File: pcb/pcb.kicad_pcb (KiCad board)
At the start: 2 copper layers, 69.8 x 69.8 mm, 61 parts, among them J1 USB_C_Receptacle_USB2.0, J2 Conn_01x05, SW1 SW_Push, SW2 SW_Push, U1 XC6206P332MR, U2 SRV05-4, U3 DRV5056A3xDBZxQ1, U4 DRV5056A3xDBZxQ1, U5 DRV5056A3xDBZxQ1, U6 RP2040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

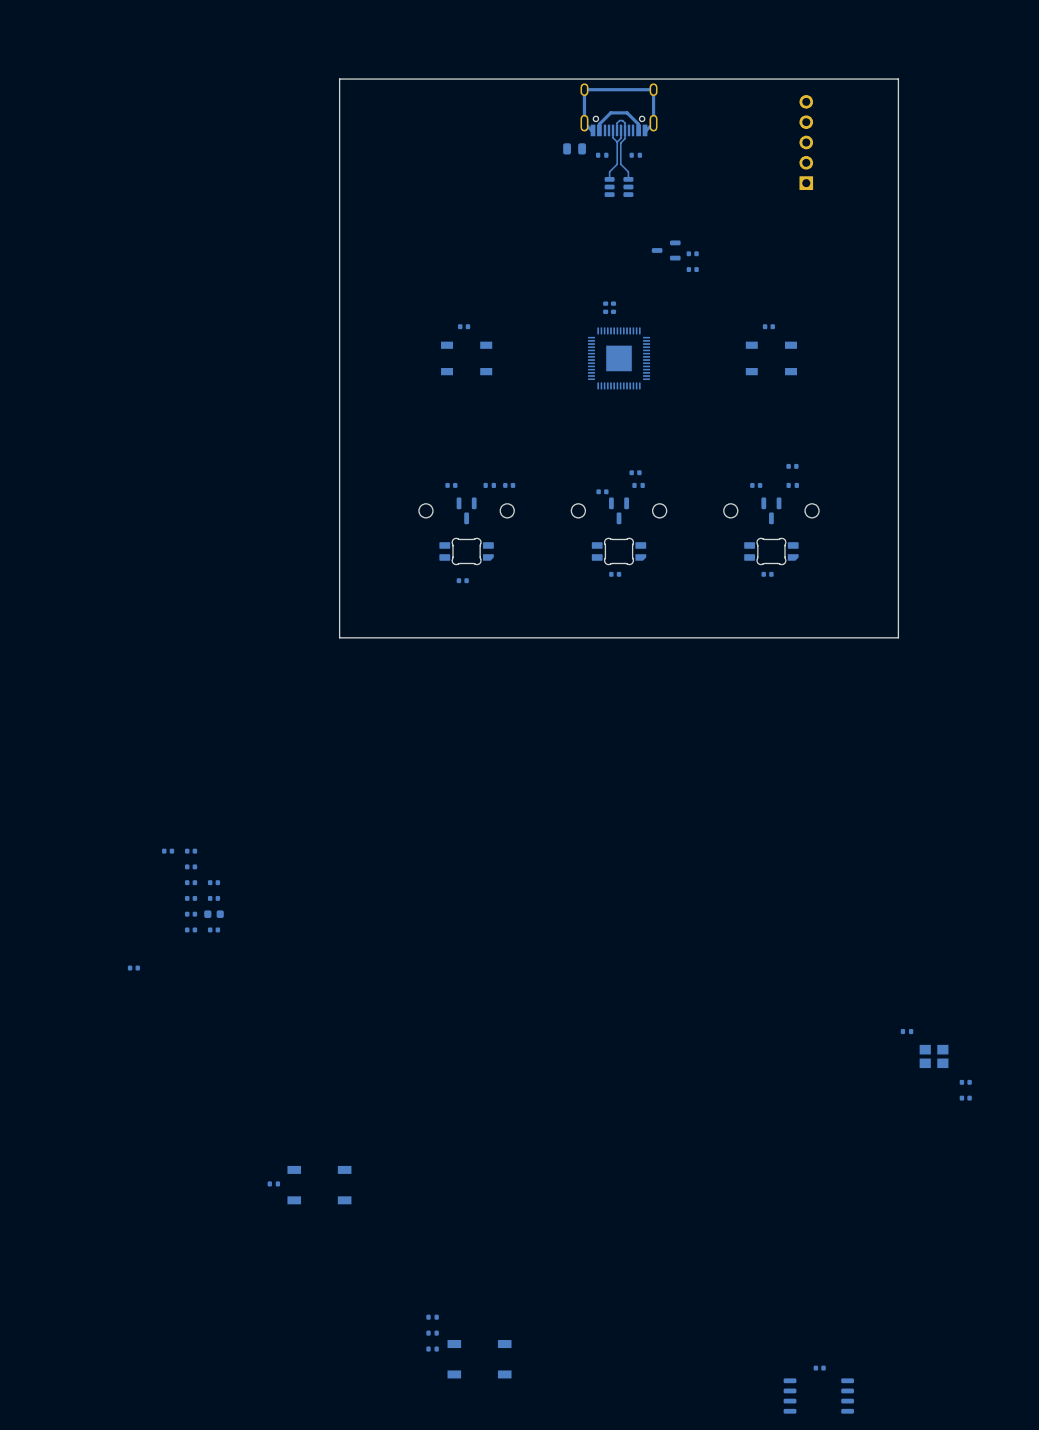
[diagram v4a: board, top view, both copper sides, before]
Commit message: feat: initial attempt at placing and routing key components
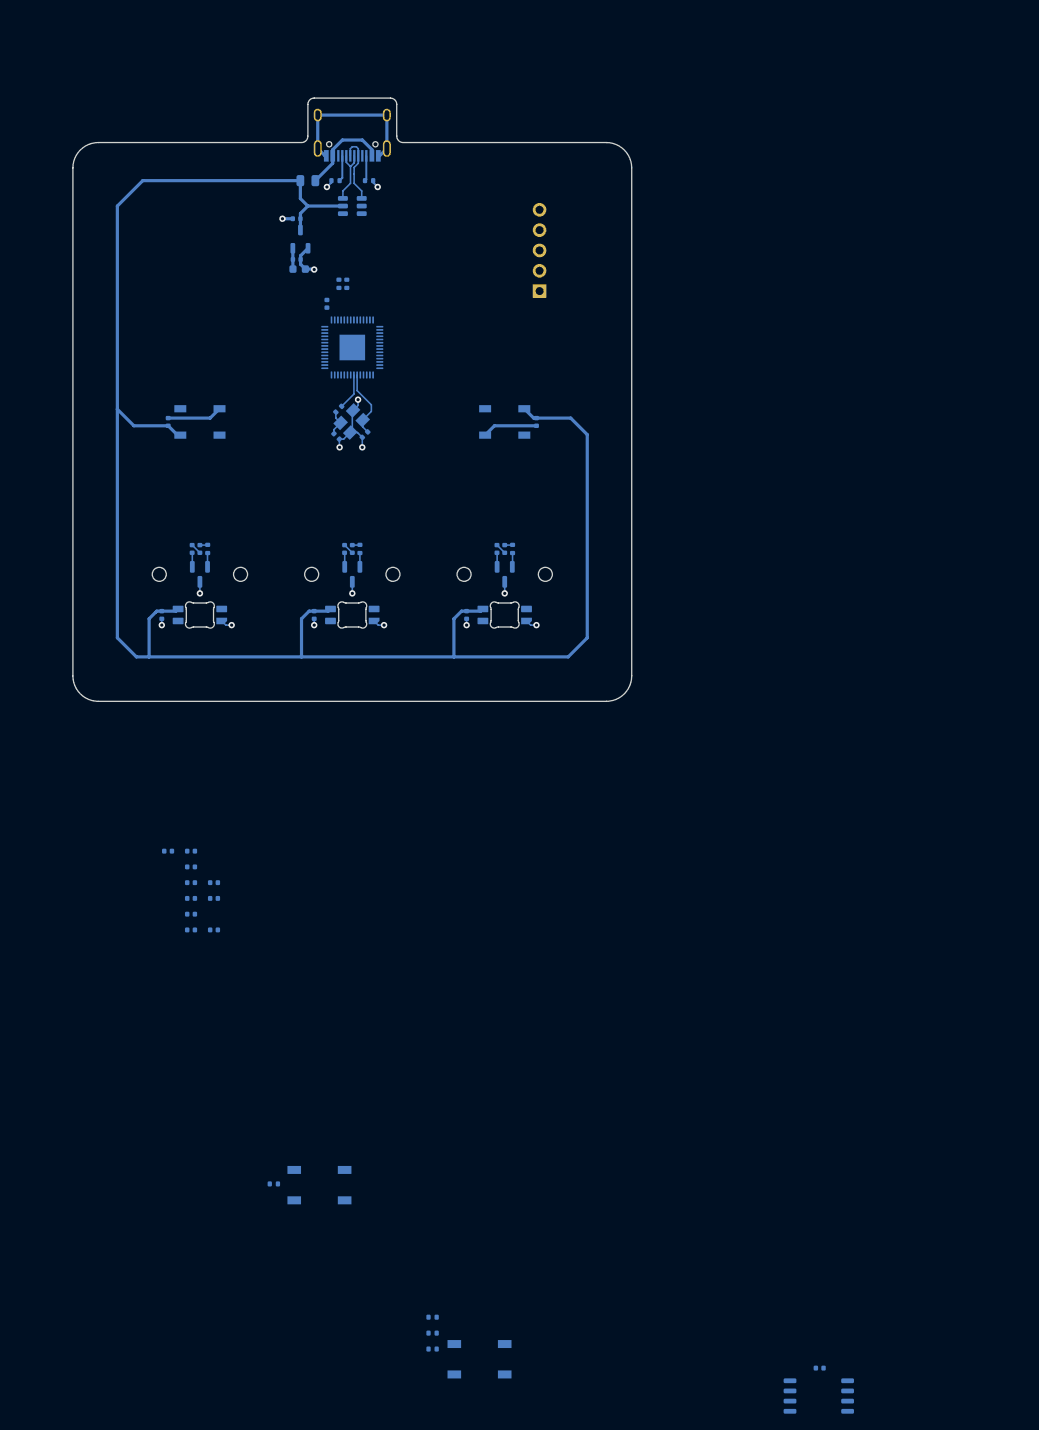
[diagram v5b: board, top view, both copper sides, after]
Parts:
- moved C25 114.1 mm to (56.8, 68.5), turned to 135 degrees
- moved C24 110.4 mm to (60.3, 68.3), turned to 45 degrees
- moved Y1 107.7 mm to (58.7, 66.6), turned to 45 degrees
- moved R7 105.3 mm to (57.0, 65.1), turned to 45 degrees
- moved C9 86.5 mm to (55.6, 51.9), turned to 90 degrees
- moved C12 81.3 mm to (52.1, 47.6), turned to 0 degrees
- moved C4 49.7 mm to (51.8, 41.3)
- moved C5 49.5 mm to (51.8, 46.4), turned to 0 degrees
- moved U1 45.7 mm to (52.3, 43.8), turned to 90 degrees
- moved C6 39.5 mm to (39.7, 82.5), turned to 90 degrees
- moved C2 38.9 mm to (35.7, 66.7), turned to -90 degrees
- moved C22 38.0 mm to (54.0, 90.8), turned to 90 degrees
- moved C27 38.0 mm to (73.0, 90.8), turned to 90 degrees
- moved C7 37.9 mm to (34.9, 90.8), turned to 90 degrees
- moved C26 37.4 mm to (77.8, 82.5), turned to 90 degrees
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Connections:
- U6 pad 38: HS0 -> HS2
- U6 pad 40: HS2 -> HS0
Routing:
- net +5V: track 0.00 -> 220.7 mm
- net GND: track 19.9 -> 66.8 mm, vias 0 -> 16
- net XIN: track 0.00 -> 8.56 mm
- net +3V3: track 0.00 -> 7.91 mm
- net XOUT: track 0.00 -> 4.56 mm
- net VBUS: track 7.62 -> 11.4 mm
- net Net-(C25-Pad2): track 0.00 -> 3.29 mm
- net Net-(J1-CC1): track 0.00 -> 3.24 mm
- net Net-(J1-CC2): track 0.00 -> 3.17 mm
- net Net-(U5-OUT): track 0.00 -> 1.74 mm
- net Net-(U3-OUT): track 0.00 -> 1.74 mm
- net Net-(U4-OUT): track 0.00 -> 1.73 mm
- net HS2: track 0.00 -> 0.99 mm
- net HS0: track 0.00 -> 0.99 mm
- net HS1: track 0.00 -> 0.96 mm
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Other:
- board size 69.8 x 69.8 mm -> 69.8 x 75.4 mm

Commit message: feat: routing for rgb leds + logic level conversion
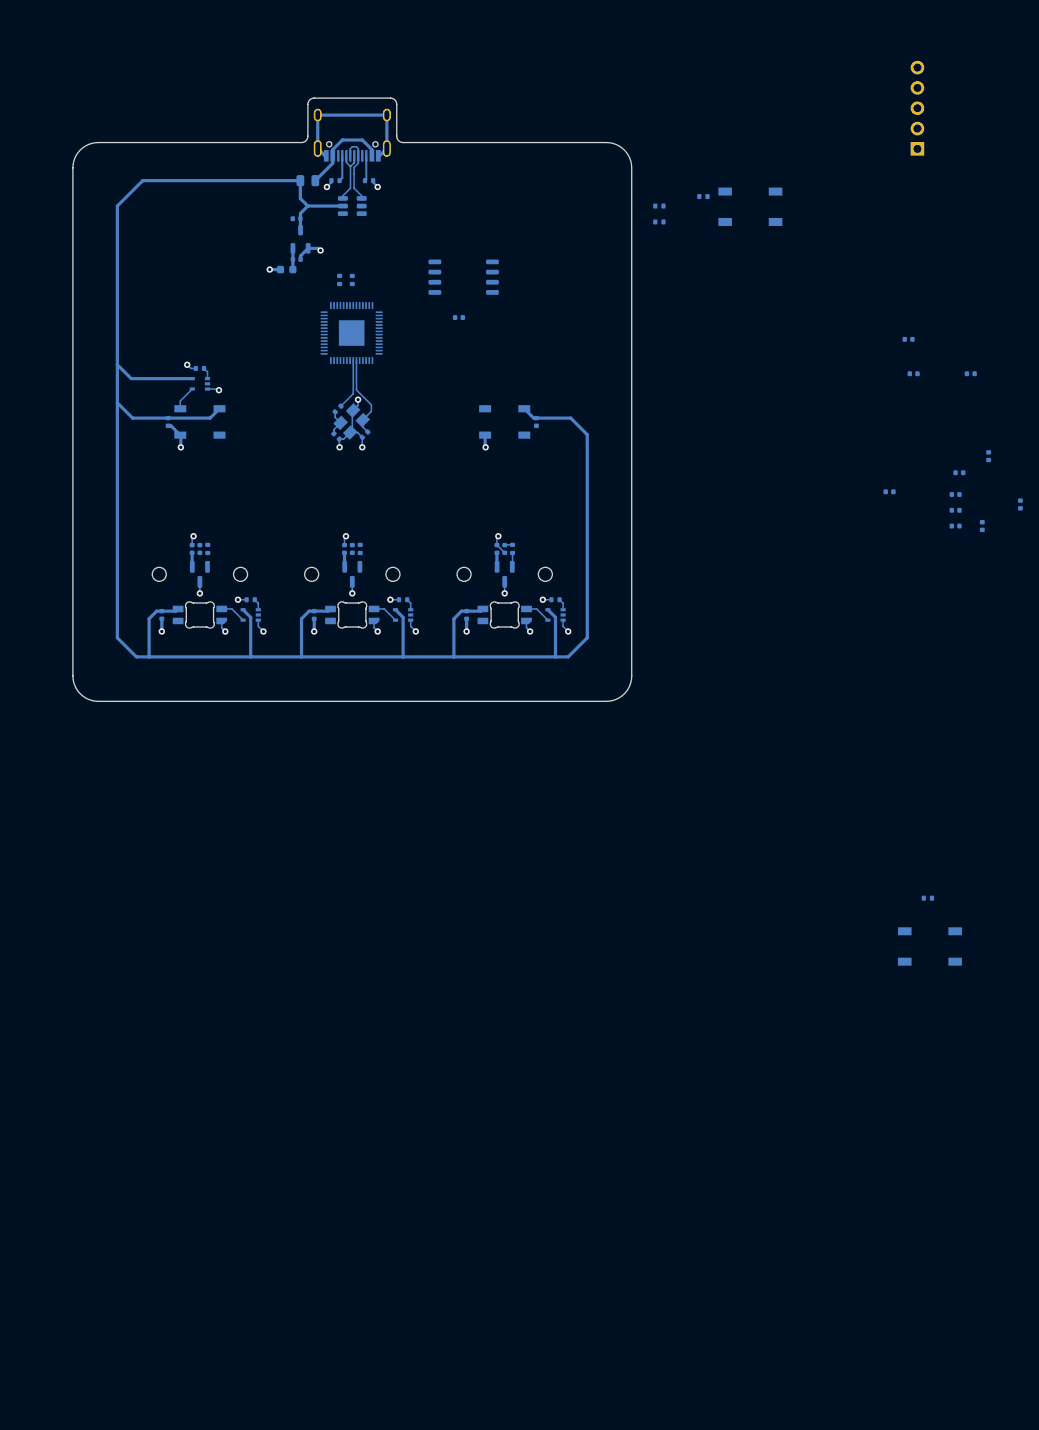
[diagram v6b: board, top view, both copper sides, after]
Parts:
- added R13: 27, Resistor_SMD:R_0402_1005Metric, B.Cu at (57.1, 48.9)
- added R14: 5k1, Resistor_SMD:R_0402_1005Metric, B.Cu at (130.7, 126.2)
- added R15: 5k1, Resistor_SMD:R_0402_1005Metric, B.Cu at (97.1, 39.7)
- added R16: 1k, Resistor_SMD:R_0402_1005Metric, B.Cu at (97.1, 41.7)
- added U10: RP2040, Package_DFN_QFN:QFN-56-1EP_7x7mm_P0.4mm_EP3.2x3.2mm, B.Cu at (58.7, 55.6)
- added U11: W25Q128JVS, Package_SO:SOIC-8_5.23x5.23mm_P1.27mm, B.Cu at (72.7, 48.6)
- added U8: 74AHCT1G125, Package_TO_SOT_SMD:SOT-353_SC-70-5, B.Cu at (84.1, 90.8)
- added U9: 74AHCT1G125, Package_TO_SOT_SMD:SOT-353_SC-70-5, B.Cu at (39.7, 61.9)
- C12: value 10uF -> 1uF; footprint Capacitor_SMD:C_0603_1608Metric -> Capacitor_SMD:C_0402_1005Metric
- C13, C21, C23, C26, C9: value 1uF -> 100nF
- C15: value 100nF -> 10uF; footprint Capacitor_SMD:C_0402_1005Metric -> Capacitor_SMD:C_0603_1608Metric
- C16, C2, C3, C7: value 100nF -> 1uF
- R10, R9: value 5k1 -> 1k
- R11: value 5k1 -> 27
- R12: value 1k -> 5k1
- R5: value 27 -> 100
- R6: value 27 -> 1k
- R8: value 100 -> 1k
- U1: value XC6206P332MR -> SRV05-4; footprint Package_TO_SOT_SMD:SOT-23-3 -> PCM_marbastlib-various:SOT-23-6-routable
- U2: value SRV05-4 -> XC6206P332MR; footprint PCM_marbastlib-various:SOT-23-6-routable -> Package_TO_SOT_SMD:SOT-23-3
- U6: value RP2040 -> 74AHCT1G125; footprint Package_DFN_QFN:QFN-56-1EP_7x7mm_P0.4mm_EP3.2x3.2mm -> Package_TO_SOT_SMD:SOT-353_SC-70-5
- U7: value W25Q128JVS -> 74AHCT1G125; footprint Package_SO:SOIC-8_5.23x5.23mm_P1.27mm -> Package_TO_SOT_SMD:SOT-353_SC-70-5
- moved R12 148.0 mm to (102.6, 38.5)
- moved SW2 148.0 mm to (108.5, 39.8)
- moved C28 138.8 mm to (72.1, 53.6)
- moved R11 132.0 mm to (58.7, 48.9), turned to -90 degrees
- moved R10 122.1 mm to (39.7, 60.0)
- moved C13 111.7 mm to (128.9, 60.6)
- moved U7 110.6 mm to (65.1, 90.8)
- moved C14 110.2 mm to (128.3, 56.4)
- moved C20 109.6 mm to (134.6, 73.0)
- moved C18 108.1 mm to (134.2, 77.7)
- moved C19 108.1 mm to (134.2, 79.7)
- moved C17 108.1 mm to (134.2, 75.7)
- moved C16 100.1 mm to (125.9, 75.4)
- moved R9 97.2 mm to (57.0, 65.1), turned to 45 degrees
- moved C22 86.6 mm to (138.3, 71.0)
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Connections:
- C10 pad 1: +1V1 -> GND
- C10 pad 2: GND -> +5V
- C11 pad 1: +1V1 -> GND
- C11 pad 2: GND -> +5V
- C12 pad 1: +3V3 -> +1V1
- C13 pad 1: +3V3 -> +1V1
- C14 pad 1: +3V3 -> +1V1
- C2 pad 1: GND -> +3V3
- C2 pad 2: +5V -> GND
- C21 pad 1: GND -> +3V3
- C21 pad 2: HS1 -> GND
- C22 pad 1: GND -> +3V3
- C22 pad 2: +5V -> GND
- C26 pad 2: HS2 -> +5V
- C3 pad 1: GND -> +3V3
- C3 pad 2: +5V -> GND
- C7 pad 2: +5V -> HS1
- C8 pad 1: +3V3 -> GND
- C8 pad 2: GND -> HS2
- C9 pad 1: +1V1 -> GND
- C9 pad 2: GND -> +5V
- D1 pad 4: RGB_GLOW -> Net-(D1-DIN)
- LED1 pad 3: RGB_HS0 -> Net-(LED1-DIN)
- LED2 pad 3: RGB_HS1 -> Net-(LED2-DIN)
- LED3 pad 3: RGB_HS2 -> Net-(LED3-DIN)
- R10 pad 1: +3V3 -> Net-(R10-Pad1)
- R10 pad 2: Net-(R10-Pad2) -> GND
- R11 pad 1: Net-(R10-Pad2) -> D+
- R11 pad 2: Q_SEL -> Net-(U10-USB_DP)
- R12 pad 1: Net-(R12-Pad1) -> +3V3
- R12 pad 2: Q_SEL -> Net-(R12-Pad2)
- R5 pad 1: D+ -> Net-(U5-OUT)
- R5 pad 2: Net-(U6-USB_DP) -> HS2
- R6 pad 1: D- -> Net-(R6-Pad1)
- R6 pad 2: Net-(U6-USB_DM) -> GND
- R7 pad 1: Net-(C25-Pad2) -> Net-(R7-Pad1)
- R7 pad 2: XOUT -> GND
- R8 pad 1: Net-(U5-OUT) -> Net-(R8-Pad1)
- R8 pad 2: HS2 -> GND
- R9 pad 1: +3V3 -> Net-(C25-Pad2)
- R9 pad 2: RESET -> XOUT
- SW2 pad 2: Net-(R12-Pad1) -> Net-(R16-Pad1)
- U1 pad 1: GND -> D+
- U1 pad 2: +3V3 -> GND
- U1 pad 3: +5V -> unconnected-(U1-IO2-Pad3)
- U2 pad 1: D+ -> GND
- U2 pad 2: GND -> +3V3
- U2 pad 3: unconnected-(U2-IO2-Pad3) -> +5V
- U6 pad 1: +3V3 -> Net-(R6-Pad1)
- U6 pad 2: RGB_GLOW -> RGB_HS0
- U6 pad 3: RGB_HS0 -> GND
- U6 pad 4: RGB_HS1 -> Net-(LED1-DIN)
- U6 pad 5: RGB_HS2 -> +5V
- U7 pad 1: Q_SEL -> Net-(R7-Pad1)
- U7 pad 2: Q_IO1 -> RGB_HS1
- U7 pad 3: Q_IO2 -> GND
- U7 pad 4: GND -> Net-(LED2-DIN)
- U7 pad 5: Q_IO0 -> +5V
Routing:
- net +5V: track 220.7 -> 254.5 mm
- net GND: track 66.8 -> 71.6 mm, vias 16 -> 29
- net Net-(LED2-DIN): track 0.00 -> 3.25 mm
- net Net-(LED1-DIN): track 0.00 -> 3.25 mm
- net Net-(LED3-DIN): track 0.00 -> 3.25 mm
- net Net-(D1-DIN): track 0.00 -> 3.08 mm
- net XIN: track 8.56 -> 10.4 mm
- net XOUT: track 4.56 -> 6.34 mm
- net Net-(U3-OUT): track 1.74 -> 0.00 mm
- net Net-(U4-OUT): track 1.73 -> 0.00 mm
- net Net-(R10-Pad1): track 0.00 -> 1.46 mm
- net Net-(R8-Pad1): track 0.00 -> 1.44 mm
- net Net-(R7-Pad1): track 0.00 -> 1.44 mm
- net Net-(R6-Pad1): track 0.00 -> 1.44 mm
- net HS0: track 0.99 -> 0.00 mm
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
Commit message: feat: most of pcb routed
still need to find a location for the debug header and reset switch, as they're kinda linked together...

after this, I can think about routing the LED logic lines and hall sensor power lines.
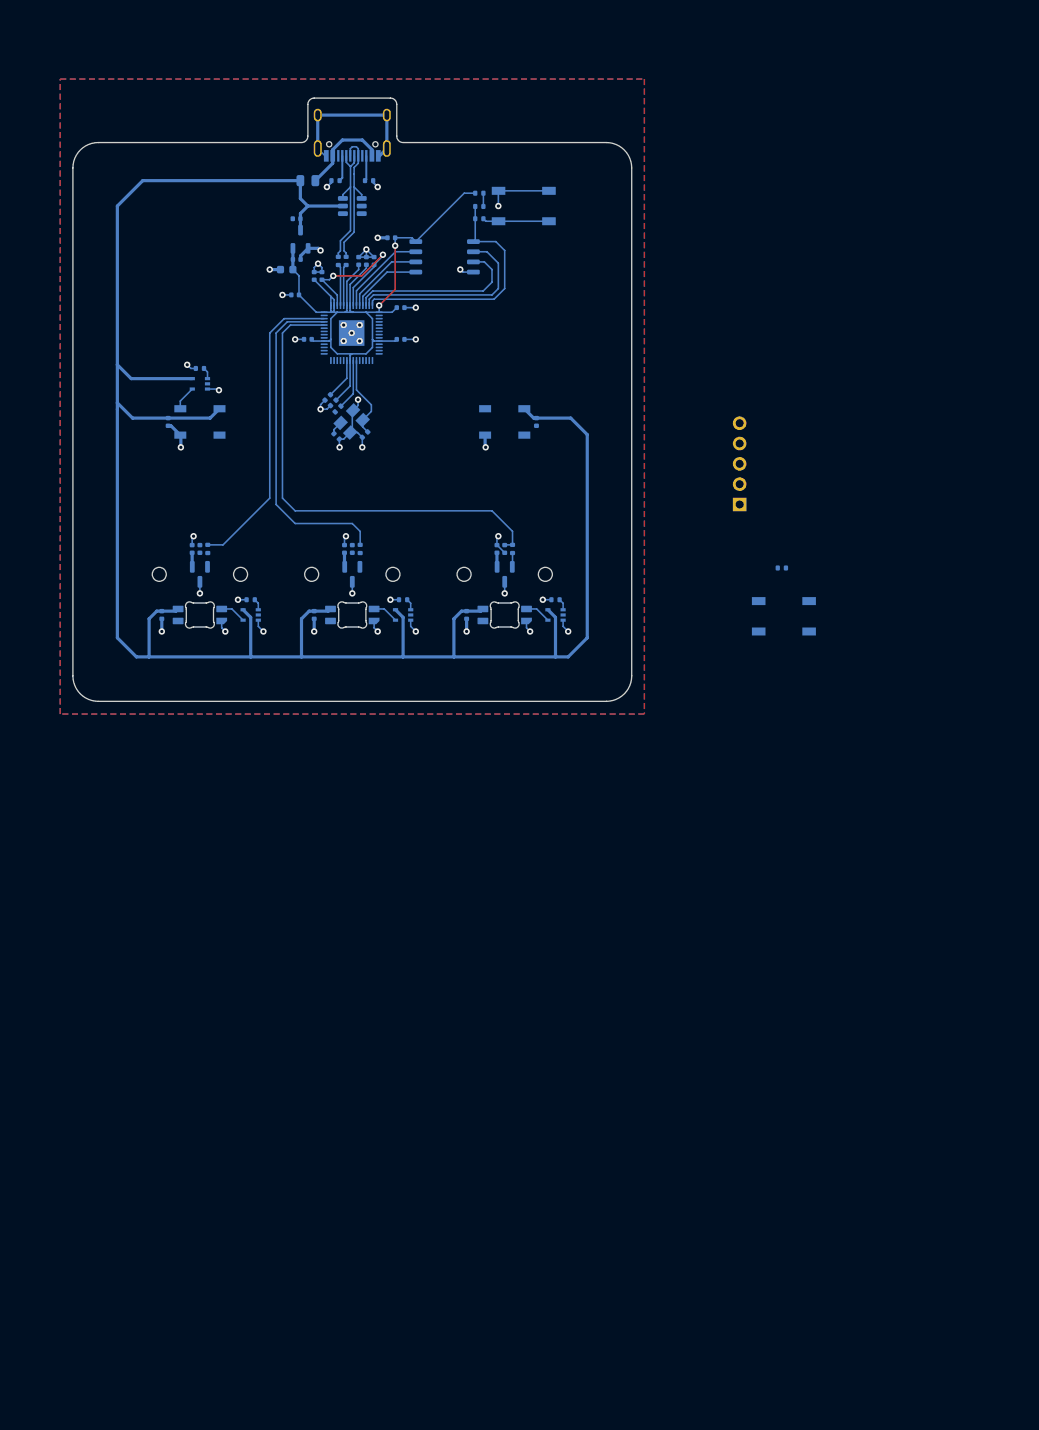
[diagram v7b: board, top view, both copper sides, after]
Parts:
- moved C21 90.6 mm to (51.6, 50.8), turned to 180 degrees
- moved C23 86.8 mm to (56.4, 64.3), turned to -135 degrees
- moved C17 83.3 mm to (53.2, 56.3)
- moved C22 82.4 mm to (59.5, 46.5)
- moved C12 82.0 mm to (54.9, 48.4), turned to 90 degrees
- moved C19 80.8 mm to (60.5, 46.5), turned to 90 degrees
- moved C16 76.8 mm to (54.0, 48.4), turned to 90 degrees
- moved C13 73.3 mm to (55.7, 63.6), turned to -135 degrees
- moved C20 72.8 mm to (64.8, 52.4), turned to 0 degrees
- moved C18 72.6 mm to (64.8, 56.4), turned to 0 degrees
- moved C14 67.5 mm to (61.5, 46.5), turned to 90 degrees
- moved J2 49.7 mm to (107.2, 77.0)
- moved R14 45.1 mm to (112.4, 84.9)
- moved SW1 45.1 mm to (112.7, 91.0)
- moved SW2 28.3 mm to (80.2, 39.7)
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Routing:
- net +3V3: track 8.00 -> 96.3 mm, vias 0 -> 2
- net HS2: track 0.99 -> 59.4 mm
- net HS1: track 0.00 -> 41.6 mm
- net HS0: track 0.00 -> 38.4 mm
- net Q_SEL: track 0.00 -> 31.4 mm
- net GND: track 71.6 -> 99.8 mm, vias 29 -> 44
- net +1V1: track 0.00 -> 25.9 mm, vias 0 -> 2
- net Q_IO1: track 0.00 -> 24.4 mm
- net Q_IO2: track 0.00 -> 21.8 mm
- net Q_IO3: track 0.00 -> 11.3 mm
- net Q_CLK: track 0.00 -> 10.1 mm
- net D-: track 7.47 -> 16.8 mm
- net D+: track 8.92 -> 18.3 mm
- net Q_IO0: track 0.00 -> 9.03 mm
- net Net-(R16-Pad1): track 0.00 -> 8.33 mm
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- added copper zone on B.Cu, net GND
- added copper zone on F.Cu, net GND
